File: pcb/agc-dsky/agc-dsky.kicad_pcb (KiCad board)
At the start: 2 copper layers, 91 x 120 mm, 152 parts, among them IC1 TPS62132, IC10 LDS-3161AX, IC11 LDS-3161AX, IC12 LDS-3161AX, IC13 LDS-3161AX, IC14 LDS-3161AX, IC15 LDS-3161AX, IC16 LDS-3161AX, IC17 LDS-3161AX, IC18 LDS-3161AX, IC19 LDS-3161AX, IC2 STM32F072RBT6, IC20 LDS-3161AX, IC21 LDS-3161AX, IC22 LDS-3161AX, IC23 LDS-3161AX, IC24 LDS-3161AX, IC25 LDS-3161AX, IC26 LDS-3161AX, IC27 WS2812B, IC28 WS2812B, IC29 WS2812B, IC3 MCP23S08, IC30 WS2812B, IC31 WS2812B, IC32 WS2812B, IC33 WS2812B, IC34 WS2812B, IC35 WS2812B, IC36 WS2812B, IC37 WS2812B, IC38 WS2812B, IC39 WS2812B, IC4 MCP23S08, IC5 MCP23S08, IC6 LDS-3161AX, IC7 LDS-3161AX, IC8 LDS-3161AX, IC9 LDS-3161AX, J1 MICROUSB, P1 SWD_TC, Q1 FDN327N, Q2 FDN327N, Q3 FDN327N, Q4 FDN327N, Q5 FDN327N, Q6 FDN327N, Q7 FDN327N, Q8 FDN327N, SW9 SKHHALA010

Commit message: Bridge separated ground plane through ALT LED and add name + date to silkscreen
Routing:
- net GND: track 298.0 -> 301.5 mm
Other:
- board text added: "Gregory Brooks 2018"
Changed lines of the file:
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@@
   (general
     (thickness 1.6)
-    (drawings 51)
-    (tracks 2258)
+    (drawings 52)
+    (tracks 2259)
     (zones 0)
     (modules 152)
@@
   )
   (setup
-    (last_trace_width 0.25)
+    (last_trace_width 0.3)
     (user_trace_width 0.2)
     (user_trace_width 0.25)
@@
     )
   )
+  (gr_text "Gregory Brooks 2018" (at 134.75 33.25) (layer F.SilkS)
+    (effects (font (size 1.5 1.5) (thickness 0.3)))
+  )
   (gr_line (start 110.5 110.25) (end 146 110.25) (layer B.SilkS) (width 0.2))
   (gr_line (start 110.5 31.5) (end 146 31.5) (layer B.SilkS) (width 0.2))
@@
   (gr_line (start 58.75 35) (end 58.75 145) (layer Edge.Cuts) (width 0.2))
   (gr_line (start 144.75 30) (end 63.75 30) (layer Edge.Cuts) (width 0.2))
+  (segment (start 114.5 93.5) (end 118 93.5) (width 0.3) (layer B.Cu) (net 2))
   (segment (start 146.75 107.5) (end 147.25 107) (width 0.3) (layer F.Cu) (net 1))
   (segment (start 146.75 113.230002) (end 146.75 107.5) (width 0.3) (layer F.Cu) (net 1))

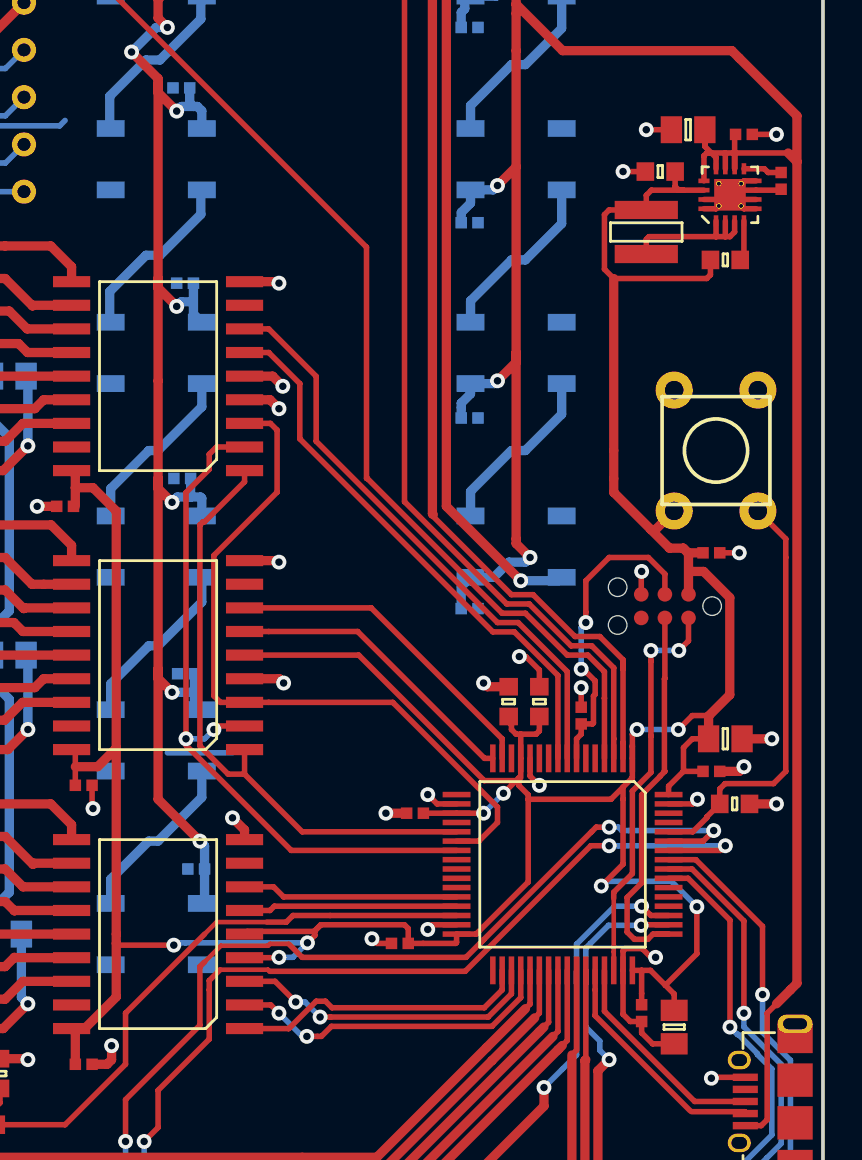
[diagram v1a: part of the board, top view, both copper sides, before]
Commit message: Thicken power traces
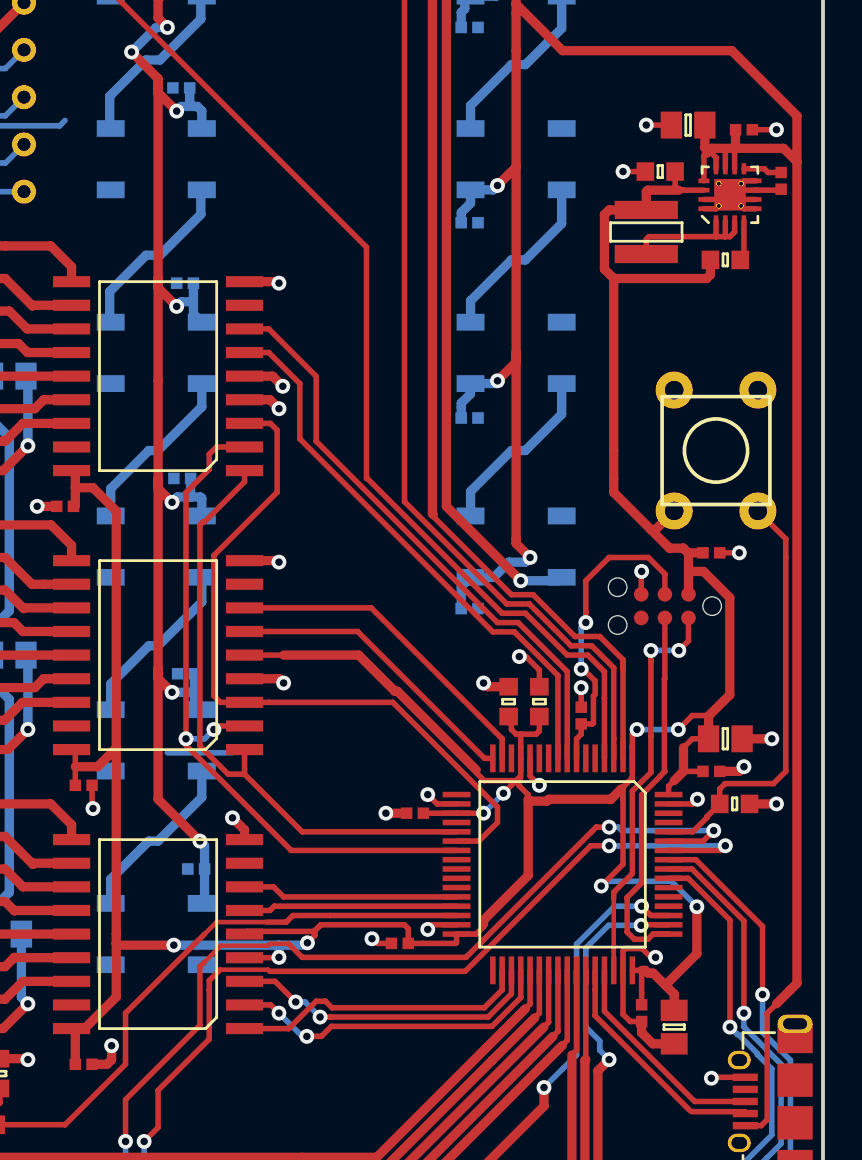
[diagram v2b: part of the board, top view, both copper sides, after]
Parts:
- moved C1 0.25 mm to (142.5, 59.8)
- moved C2 0.25 mm to (145.5, 60.0)
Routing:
- net 3v3: track 200.7 -> 203.5 mm

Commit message: Tidy up button references
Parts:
- SW20: renamed from KEY REL
- renumbered + to SW1, 8 to SW10, 5 to SW11, 2 to SW12, ENTR to SW13, 9 to SW14, 6 to SW15, 3 to SW16, RSET to SW17, CLR to SW18, PRO to SW19, - to SW2, 0 to SW3, VERB to SW4, 7 to SW5, 4 to SW6, 1 to SW7, NOUN to SW8
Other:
- board text added: "+"
- board text added: "-"
- board text added: "0"
- board text added: "1"
- board text added: "2"
- board text added: "3"
- board text added: "4"
- board text added: "5"
- board text added: "6"
- board text added: "7"
- board text added: "8"
- board text added: "9"
- board text added: "CLR"
- board text added: "ENTR"
- board text added: "PRO"
- board text added: "RSET"
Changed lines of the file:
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@@
   (general
     (thickness 1.6)
-    (drawings 52)
+    (drawings 71)
     (tracks 2278)
     (zones 0)
@@
   )
   (setup
-    (last_trace_width 0.5)
+    (last_trace_width 0.25)
     (user_trace_width 0.2)
     (user_trace_width 0.25)
@@
   (module agc-dsky:SKPM (layer B.Cu)
     (at 126.25 121.5 180)
-    (fp_text reference + (at 0 -4.5 180) (layer B.SilkS)
+    (fp_text reference SW1 (at 0 -4.5 180) (layer B.Fab)
       (effects (font (size 1.5 1.5) (thickness 0.3)) (justify mirror))
     )
@@
   (module agc-dsky:SKPM (layer B.Cu)
     (at 126.25 132.5 180)
-    (fp_text reference - (at 0 -4.5 180) (layer B.SilkS)
+    (fp_text reference SW2 (at 0 -4.5 180) (layer B.Fab)
       (effects (font (size 1.5 1.5) (thickness 0.3)) (justify mirror))
     )
@@
   (module agc-dsky:SKPM (layer B.Cu)
     (at 126.25 143.5 180)
-    (fp_text reference 0 (at 0 -5 180) (layer B.SilkS)
+    (fp_text reference SW3 (at 0 -5 180) (layer B.Fab)
       (effects (font (size 1.5 1.5) (thickness 0.3)) (justify mirror))
     )
@@
   (module agc-dsky:SKPM (layer B.Cu)
     (at 137.25 127.5 180)
-    (fp_text reference VERB (at 0 -4.75 180) (layer B.SilkS)
+    (fp_text reference SW4 (at 0 -4.75 180) (layer B.Fab)
       (effects (font (size 1.5 1.5) (thickness 0.3)) (justify mirror))
     )
@@
   (module agc-dsky:SKPM (layer B.Cu)
     (at 115.25 121.5 180)
-    (fp_text reference 7 (at 0 -5 180) (layer B.SilkS)
+    (fp_text reference SW5 (at 0 -5 180) (layer B.Fab)
       (effects (font (size 1.5 1.5) (thickness 0.3)) (justify mirror))
     )
@@
   (module agc-dsky:SKPM (layer B.Cu)
     (at 115.25 132.5 180)
-    (fp_text reference 4 (at 0 -5 180) (layer B.SilkS)
+    (fp_text reference SW6 (at 0 -5 180) (layer B.Fab)
       (effects (font (size 1.5 1.5) (thickness 0.3)) (justify mirror))
     )
@@
   (module agc-dsky:SKPM (layer B.Cu)
     (at 115.25 143.5 180)
-    (fp_text reference 1 (at 0 -5 180) (layer B.SilkS)
+    (fp_text reference SW7 (at 0 -5 180) (layer B.Fab)
       (effects (font (size 1.5 1.5) (thickness 0.3)) (justify mirror))
     )
@@
   (module agc-dsky:SKPM (layer B.Cu)
     (at 137.25 138.5 180)
-    (fp_text reference NOUN (at 0 -5 180) (layer B.SilkS)
+    (fp_text reference SW8 (at 0 -5 180) (layer B.Fab)
       (effects (font (size 1.5 1.5) (thickness 0.3)) (justify mirror))
     )
@@
   (module agc-dsky:SKPM (layer B.Cu)
     (at 104.25 121.5 180)
-    (fp_text reference 8 (at 0 -5 180) (layer B.SilkS)
+    (fp_text reference SW10 (at 0 -5 180) (layer B.Fab)
       (effects (font (size 1.5 1.5) (thickness 0.3)) (justify mirror))
     )
@@
   (module agc-dsky:SKPM (layer B.Cu)
     (at 104.25 132.5 180)
-    (fp_text reference 5 (at 0 -5 180) (layer B.SilkS)
+    (fp_text reference SW11 (at 0 -5 180) (layer B.Fab)
       (effects (font (size 1.5 1.5) (thickness 0.3)) (justify mirror))
     )
@@
   (module agc-dsky:SKPM (layer B.Cu)
     (at 104.25 143.5 180)
-    (fp_text reference 2 (at 0 -5 180) (layer B.SilkS)
+    (fp_text reference SW12 (at 0 -5 180) (layer B.Fab)
       (effects (font (size 1.5 1.5) (thickness 0.3)) (justify mirror))
     )
@@
   (module agc-dsky:SKPM (layer B.Cu)
     (at 71.25 127.5 180)
-    (fp_text reference ENTR (at 0 -5 180) (layer B.SilkS)
+    (fp_text reference SW13 (at 0 -5 180) (layer B.Fab)
       (effects (font (size 1.5 1.5) (thickness 0.3)) (justify mirror))
     )
@@
   (module agc-dsky:SKPM (layer B.Cu)
     (at 93.25 121.5 180)
-    (fp_text reference 9 (at 0 -5 180) (layer B.SilkS)
+    (fp_text reference SW14 (at 0 -5 180) (layer B.Fab)
       (effects (font (size 1.5 1.5) (thickness 0.3)) (justify mirror))
     )
@@
   (module agc-dsky:SKPM (layer B.Cu)
     (at 93.25 132.5 180)
-    (fp_text reference 6 (at 0 -5 180) (layer B.SilkS)
+    (fp_text reference SW15 (at 0 -5 180) (layer B.Fab)
       (effects (font (size 1.5 1.5) (thickness 0.3)) (justify mirror))
     )
@@
   (module agc-dsky:SKPM (layer B.Cu)
     (at 93.25 143.5 180)
-    (fp_text reference 3 (at 0 -5 180) (layer B.SilkS)
+    (fp_text reference SW16 (at 0 -5 180) (layer B.Fab)
       (effects (font (size 1.5 1.5) (thickness 0.3)) (justify mirror))
     )
@@
   (module agc-dsky:SKPM (layer B.Cu)
     (at 71.25 138.5 180)
-    (fp_text reference RSET (at 0 -5 180) (layer B.SilkS)
+    (fp_text reference SW17 (at 0 -5 180) (layer B.Fab)
       (effects (font (size 1.5 1.5) (thickness 0.3)) (justify mirror))
     )
@@
   (module agc-dsky:SKPM (layer B.Cu)
     (at 82.25 121.5 180)
-    (fp_text reference CLR (at 0 -5 180) (layer B.SilkS)
+    (fp_text reference SW18 (at 0 -5 180) (layer B.Fab)
       (effects (font (size 1.5 1.5) (thickness 0.3)) (justify mirror))
     )
@@
   (module agc-dsky:SKPM (layer B.Cu)
     (at 82.25 132.5 180)
-    (fp_text reference PRO (at 0 -5 180) (layer B.SilkS)
+    (fp_text reference SW19 (at 0 -5 180) (layer B.Fab)
       (effects (font (size 1.5 1.5) (thickness 0.3)) (justify mirror))
     )
@@
   (module agc-dsky:SKPM (layer B.Cu)
     (at 82.25 143.5 180)
-    (fp_text reference "KEY REL" (at 0 -5 180) (layer B.SilkS)
+    (fp_text reference SW20 (at 0 -5 180) (layer B.Fab)
       (effects (font (size 1.5 1.5) (thickness 0.3)) (justify mirror))
     )
@@
     )
   )
+  (gr_text VERB (at 137.25 132.25) (layer B.SilkS)
+    (effects (font (size 1.5 1.5) (thickness 0.3)) (justify mirror))
+  )
+  (gr_text NOUN (at 137.25 143.5) (layer B.SilkS)
+    (effects (font (size 1.5 1.5) (thickness 0.3)) (justify mirror))
+  )
+  (gr_text RSET (at 71.25 143.5) (layer B.SilkS)
+    (effects (font (size 1.5 1.5) (thickness 0.3)) (justify mirror))
+  )
+  (gr_text ENTR (at 71.25 132.5) (layer B.SilkS)
+    (effects (font (size 1.5 1.5) (thickness 0.3)) (justify mirror))
+  )
+  (gr_text "KEY REL" (at 82.25 148.5) (layer B.SilkS)
+    (effects (font (size 1.5 1.5) (thickness 0.3)) (justify mirror))
+  )
+  (gr_text PRO (at 82.25 137.5) (layer B.SilkS)
+    (effects (font (size 1.5 1.5) (thickness 0.3)) (justify mirror))
+  )
+  (gr_text CLR (at 82.25 126.5) (layer B.SilkS)
+    (effects (font (size 1.5 1.5) (thickness 0.3)) (justify mirror))
+  )
+  (gr_text 3 (at 93.25 148.5) (layer B.SilkS)
+    (effects (font (size 1.5 1.5) (thickness 0.3)) (justify mirror))
+  )
+  (gr_text 6 (at 93.25 137.5) (layer B.SilkS)
+    (effects (font (size 1.5 1.5) (thickness 0.3)) (justify mirror))
+  )
+  (gr_text 9 (at 93.25 126.5) (layer B.SilkS)
+    (effects (font (size 1.5 1.5) (thickness 0.3)) (justify mirror))
+  )
+  (gr_text 2 (at 104.25 148.5) (layer B.SilkS)
+    (effects (font (size 1.5 1.5) (thickness 0.3)) (justify mirror))
+  )
+  (gr_text 5 (at 104.25 137.5) (layer B.SilkS)
+    (effects (font (size 1.5 1.5) (thickness 0.3)) (justify mirror))
+  )
+  (gr_text 8 (at 104.25 126.5) (layer B.SilkS)
+    (effects (font (size 1.5 1.5) (thickness 0.3)) (justify mirror))
+  )
+  (gr_text 7 (at 115.25 126.5) (layer B.SilkS)
+    (effects (font (size 1.5 1.5) (thickness 0.3)) (justify mirror))
+  )
+  (gr_text 4 (at 115.25 137.5) (layer B.SilkS)
+    (effects (font (size 1.5 1.5) (thickness 0.3)) (justify mirror))
+  )
+  (gr_text 1 (at 115.25 148.5) (layer B.SilkS)
+    (effects (font (size 1.5 1.5) (thickness 0.3)) (justify mirror))
+  )
+  (gr_text 0 (at 126.25 148.5) (layer B.SilkS)
+    (effects (font (size 1.5 1.5) (thickness 0.3)))
+  )
+  (gr_text - (at 126.25 137) (layer B.SilkS)
+    (effects (font (size 1.5 1.5) (thickness 0.3)))
+  )
+  (gr_text + (at 126.25 126) (layer B.SilkS)
+    (effects (font (size 1.5 1.5) (thickness 0.3)))
+  )
   (gr_text "Gregory Brooks 2018" (at 134.75 33.25) (layer F.SilkS)
     (effects (font (size 1.5 1.5) (thickness 0.3)))
@@
   (gr_line (start 58.75 35) (end 58.75 145) (layer Edge.Cuts) (width 0.2))
   (gr_line (start 144.75 30) (end 63.75 30) (layer Edge.Cuts) (width 0.2))
-  (segment (start 114.5 93.5) (end 118 93.5) (width 0.3) (layer B.Cu) (net 2))
   (segment (start 146.75 107.5) (end 147.25 107) (width 0.3) (layer F.Cu) (net 1))
   (segment (start 146.75 113.230002) (end 146.75 107.5) (width 0.3) (layer F.Cu) (net 1))
@@
   (segment (start 147.630002 61) (end 145 61) (width 0.5) (layer F.Cu) (net 1))
   (segment (start 145 61) (end 143.75 61) (width 0.5) (layer F.Cu) (net 1))
+  (segment (start 114.5 93.5) (end 118 93.5) (width 0.3) (layer B.Cu) (net 2))
   (segment (start 69.060001 90.140001) (end 69.71 90.79) (width 0.3) (layer B.Cu) (net 2) (status 20))
   (segment (start 68.709999 89.789999) (end 69.060001 90.140001) (width 0.3) (layer B.Cu) (net 2))

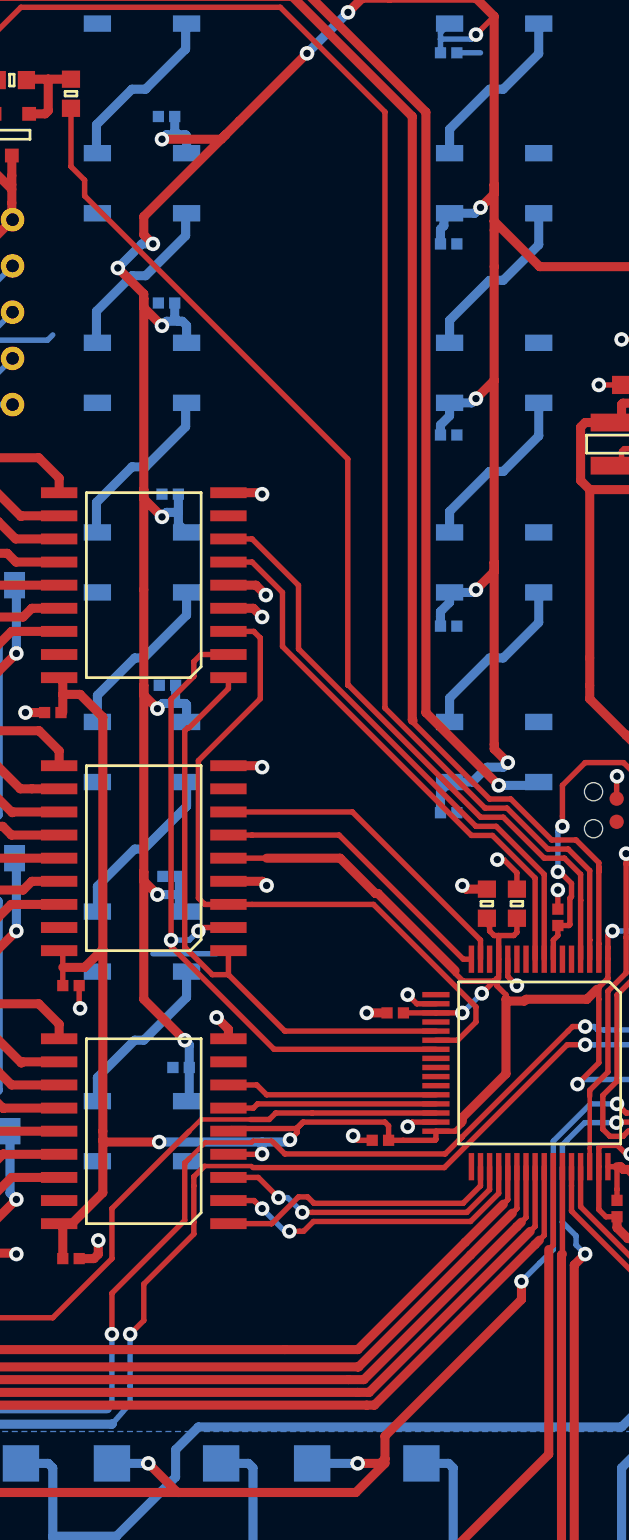
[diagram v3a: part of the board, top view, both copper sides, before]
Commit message: Add UART header and imu
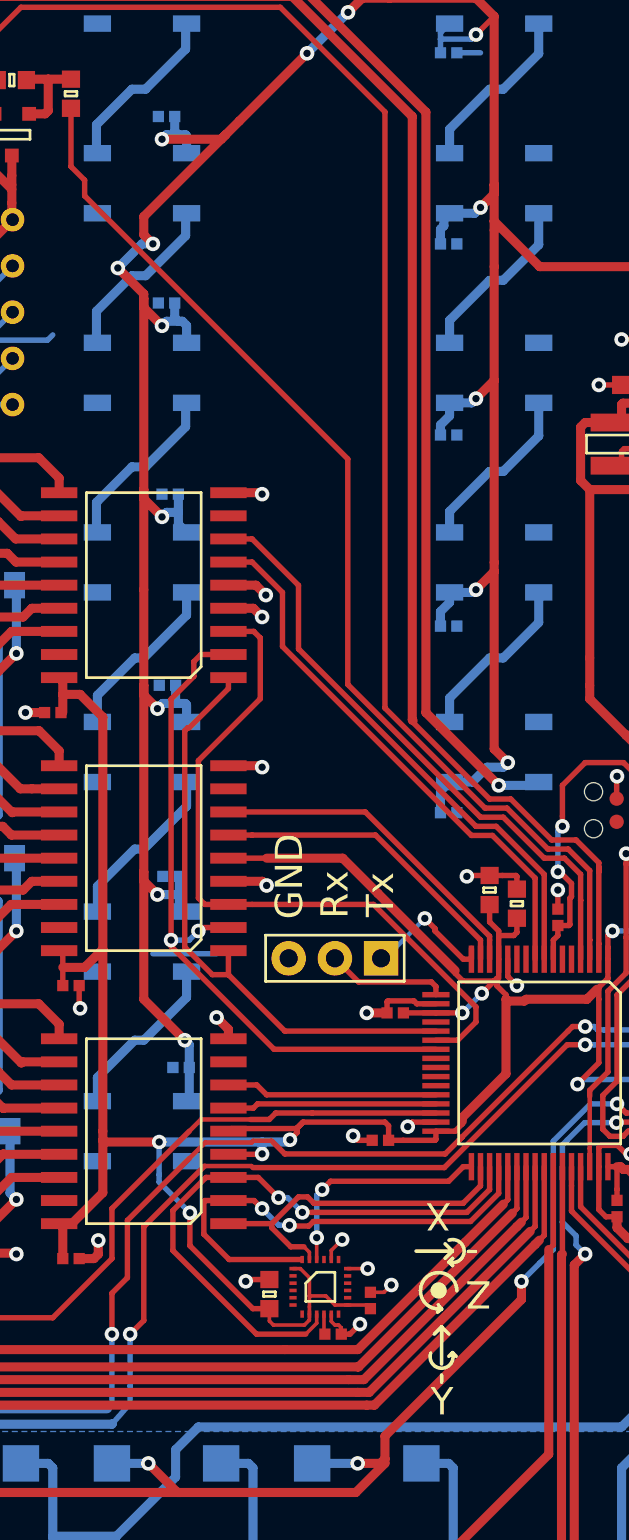
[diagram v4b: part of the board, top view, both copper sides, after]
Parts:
- added C31: 100nF, agg:0402, F.Cu at (126.5, 112.5)
- added C32: 10nF, agg:0603, F.Cu at (120.9, 112.2)
- added C33: 100nF, agg:0402, F.Cu at (124.4, 114.4)
- added IC40: MPU-9250, agg:QFN-24-MPU9250, F.Cu at (123.7, 111.8)
- added J2: CONN_01x03, agg:SIL-254P-03, F.Cu at (124.5, 93.8)
- moved C9 0.76 mm to (133.0, 90.0)
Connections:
- IC2 pad 14: (no net) -> /NCS_2
- IC2 pad 15: /NCS_2 -> /NRST_2
- IC2 pad 16: /NRST_2 -> Net-(IC2-Pad16)
- IC2 pad 17: (no net) -> Net-(IC2-Pad17)
- IC2 pad 33: (no net) -> /NCS_MPU
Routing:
- net 3v3: track 203.5 -> 226.3 mm, vias 9 -> 10
- net /SPI2_SO: track 17.6 -> 34.2 mm
- net /NCS_MPU: track 0.00 -> 12.7 mm, vias 0 -> 2
- net GND: track 301.5 -> 310.7 mm, vias 36 -> 39
- net /SPI2_SI: track 17.9 -> 26.7 mm
- net Net-(IC2-Pad16): track 0.00 -> 7.47 mm, vias 0 -> 1
- net Net-(IC2-Pad17): track 0.00 -> 6.64 mm
- net /SPI2_SCK: track 16.1 -> 19.3 mm
- net Net-(C33-Pad1): track 0.00 -> 1.12 mm
- net /NRST_2: track 16.2 -> 17.3 mm
- net /NCS_2: track 17.8 -> 18.4 mm
- net 5v: track 299.6 -> 299.1 mm
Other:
- rule pad_to_mask_clearance: 0.2 -> 0
- board text added: "GND"
- board text added: "Rx"
- board text added: "Tx"
- board text added: "X"
- board text added: "Y"
- board text added: "Z"
